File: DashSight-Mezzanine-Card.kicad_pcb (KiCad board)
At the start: 2 copper layers, 75.1 x 78.5 mm, 70 parts, among them IC1 XM1110, IC2 ELM327, J1 Pi2 Connector, J2 Euler Connector, J3 Conn_Coaxial, J4 OBD2-DB9_Male, Q1 2N3904, Q2 2N3906, Q3 2N3906, Q4 2N3904, Q5 2N3904, Q6 2N3904, Q7 2N3904, U1 MCP2561-E/P, U2 LM317L_TO92, U3 LM1085-5.0, U4 ADuM1201AR, Y1 4.0MHz

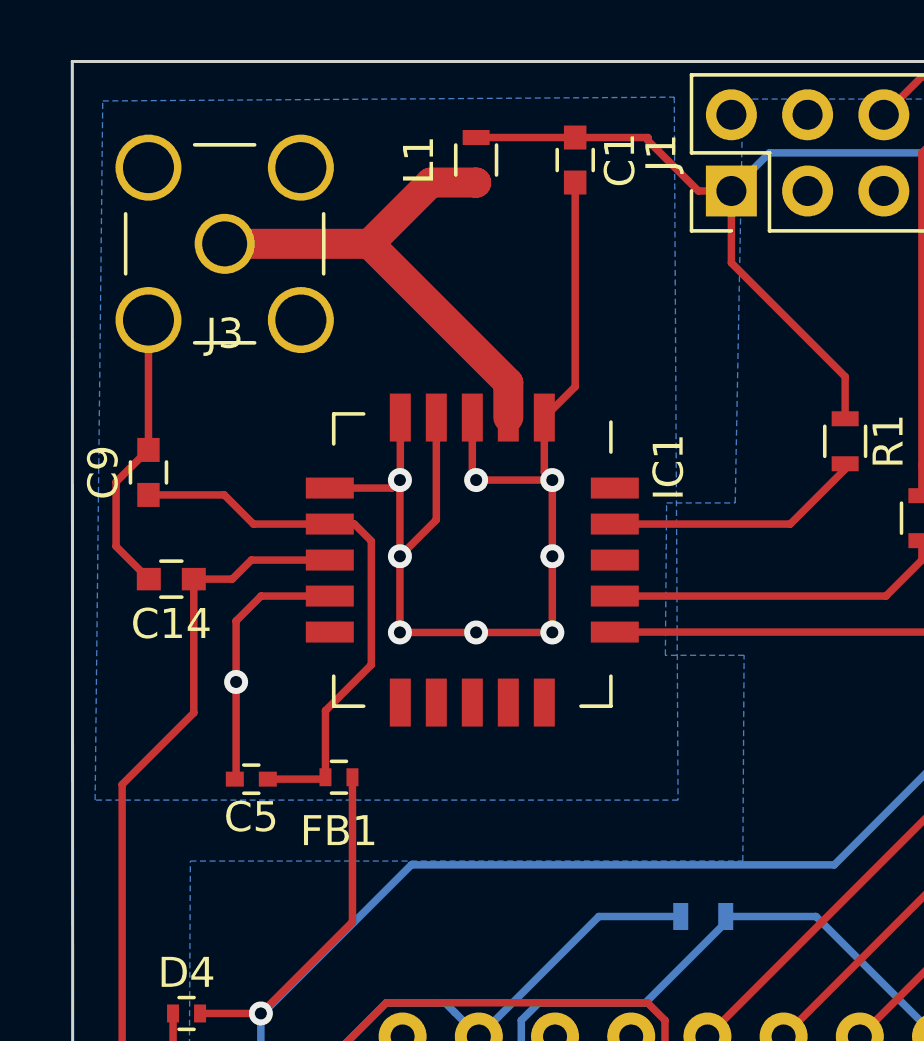
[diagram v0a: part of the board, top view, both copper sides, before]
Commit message: pcb: Update GPS layout
Signed-off-by: Alistair Francis <alistair@alistair23.me>
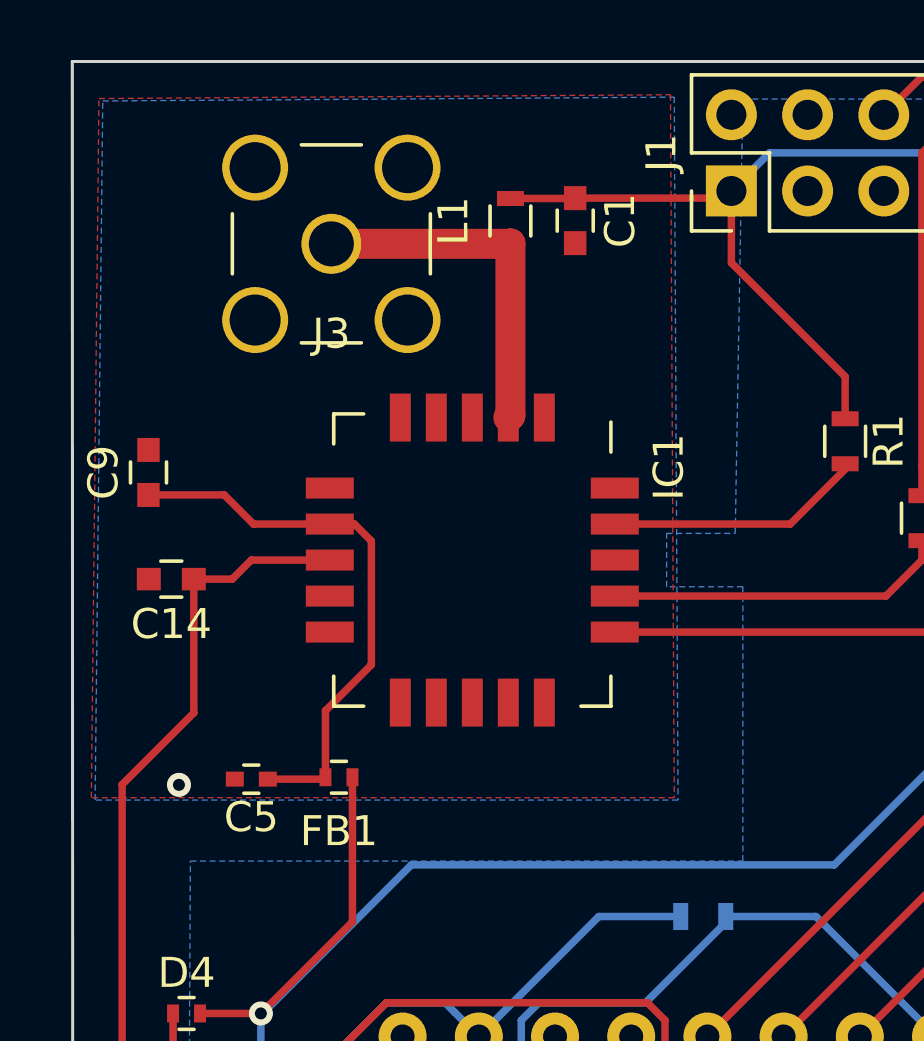
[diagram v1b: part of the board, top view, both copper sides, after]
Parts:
- moved J3 3.56 mm to (133.6, 52.6)
- moved L1 2.33 mm to (139.6, 51.8)
- moved C1 2.02 mm to (141.7, 51.8)
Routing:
- net GND: track 345.5 -> 287.2 mm, vias 17 -> 9
- net Net-(IC1-Pad2): track 16.9 -> 11.8 mm
- net +3V3: track 150.9 -> 149.1 mm
- added copper zone on F.Cu, net GND

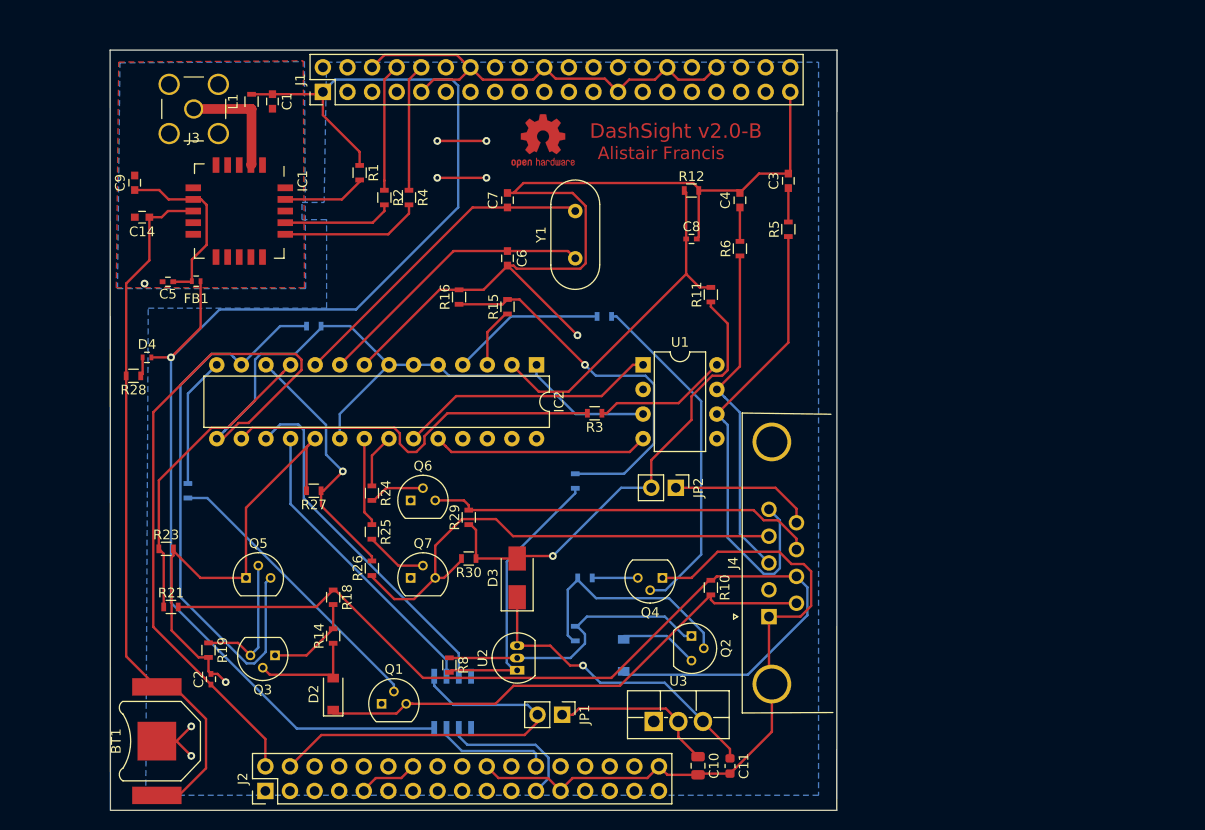
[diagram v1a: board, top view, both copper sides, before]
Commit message: pcb: Consolidate PCB layout
Signed-off-by: Alistair Francis <alistair@alistair23.me>
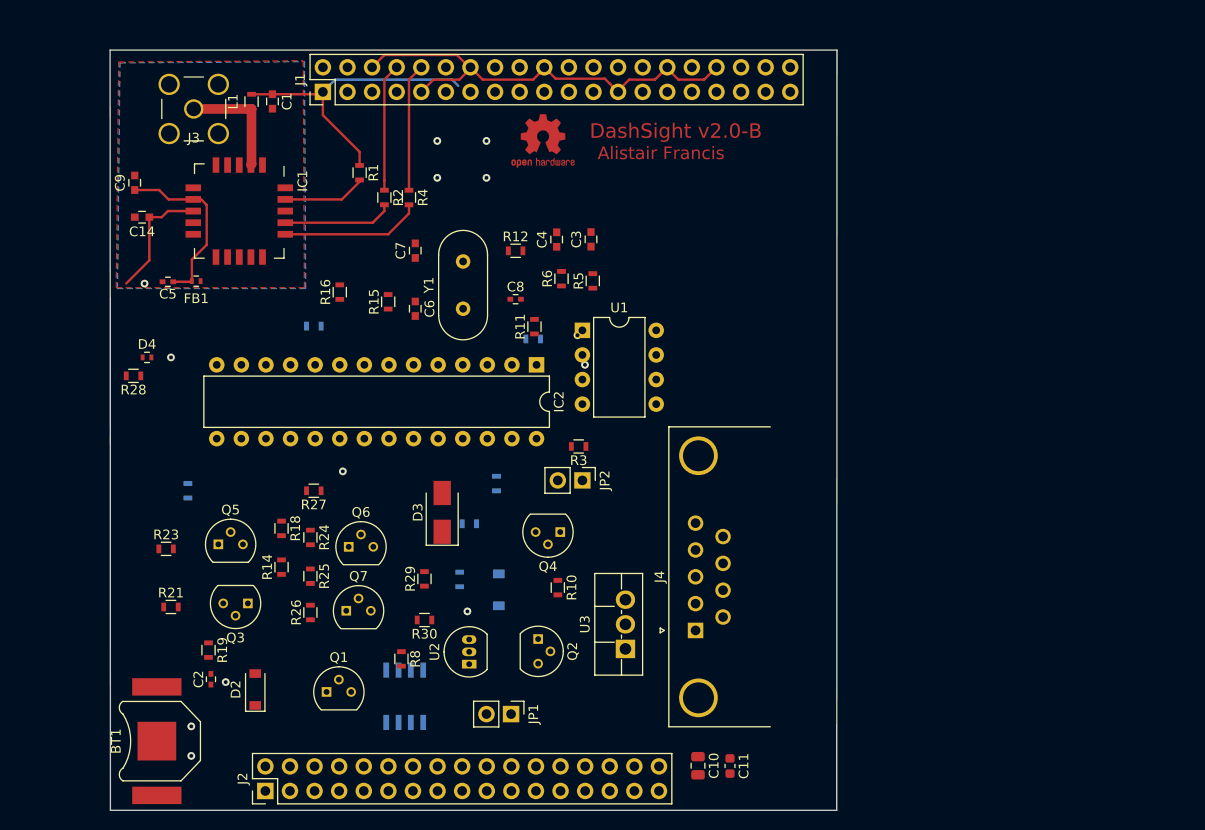
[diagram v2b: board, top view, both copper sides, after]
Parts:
- J4: footprint DashSight-PCB-Footprints:OBD2-Connector -> Connector_Dsub:DSUB-9_Male_Horizontal_P2.77x2.84mm_EdgePinOffset4.94mm_Housed_MountingHolesOffset7.48mm
- moved C3 21.3 mm to (174.6, 66.0)
- moved R5 20.9 mm to (174.8, 70.3)
- moved C4 19.4 mm to (171.1, 66.1)
- moved C8 19.2 mm to (166.8, 72.2)
- moved R12 19.2 mm to (166.8, 67.2)
- moved R6 18.7 mm to (171.6, 70.1)
- moved R11 18.5 mm to (168.8, 75.1)
- moved Q2 15.8 mm to (169.2, 107.3)
- moved R10 15.8 mm to (171.2, 102.0)
- moved D1 14.6 mm to (165.1, 102.2)
- moved R17 13.2 mm to (162.1, 95.4)
- moved R9 13.2 mm to (161.1, 101.2)
- moved Y1 12.7 mm to (161.4, 73.2)
- moved R15 12.3 mm to (153.7, 72.5)
- moved R16 12.3 mm to (148.7, 71.5)
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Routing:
- net GND: track 287.2 -> 47.4 mm, vias 9 -> 8
- net +5V: track 179.4 -> 0.00 mm
- net +3V3: track 149.1 -> 31.4 mm
- net J1850_Bus+: track 98.7 -> 0.00 mm
- net Net-(BT1-Pad1): track 73.4 -> 12.6 mm
- net Net-(IC2-Pad13): track 58.4 -> 0.00 mm
- net J1850_Bus-: track 54.5 -> 0.00 mm
- net ISO9141-2_K: track 51.8 -> 0.00 mm
- net Vbat: track 48.8 -> 0.00 mm, vias 1 -> 0
- net CAN_Low: track 48.3 -> 0.00 mm
- net ISO9141-2_L: track 40.4 -> 0.00 mm
- net PwrCntrl: track 40.0 -> 0.00 mm
- net Net-(R13-Pad2): track 39.5 -> 0.00 mm
- net Net-(IC2-Pad17): track 36.8 -> 0.00 mm
- net Net-(C8-Pad1): track 36.0 -> 0.00 mm
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
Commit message: pcb: Shrink the board
Signed-off-by: Alistair Francis <alistair@alistair23.me>
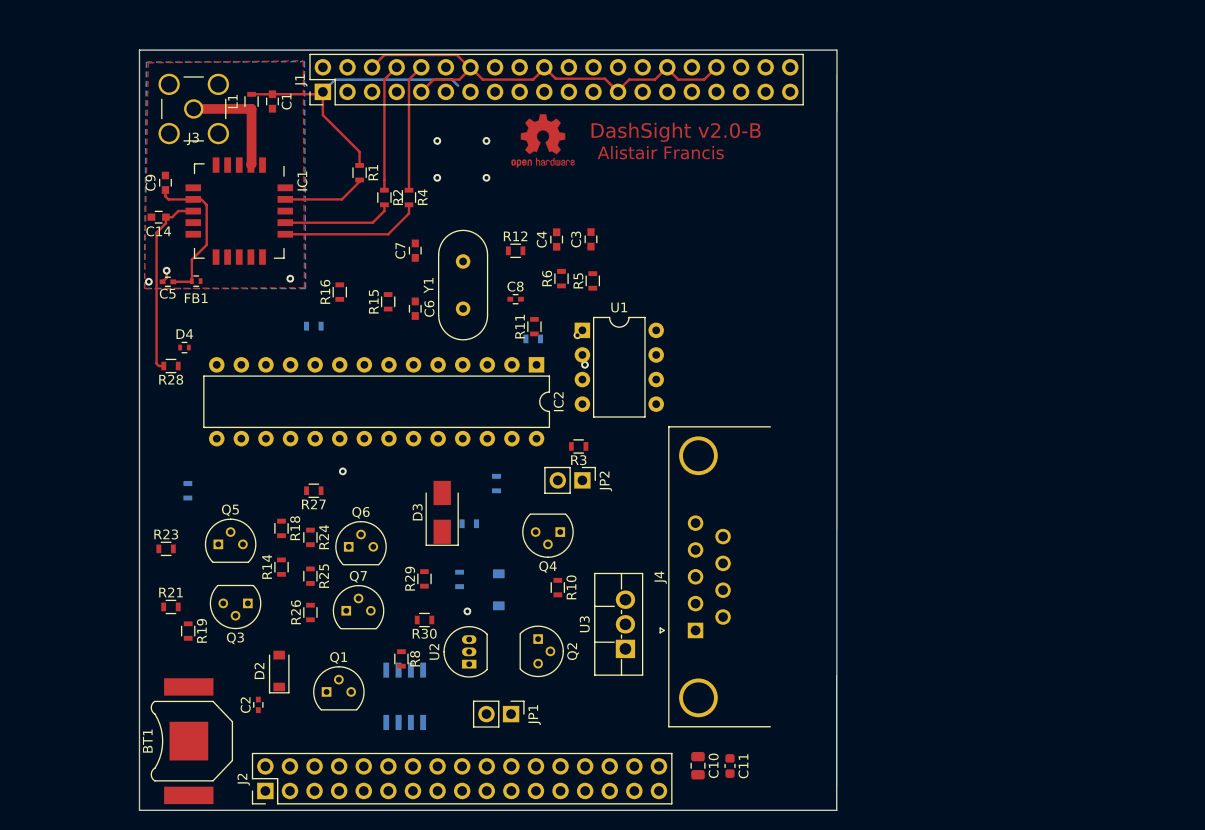
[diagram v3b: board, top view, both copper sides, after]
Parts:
- moved C2 5.56 mm to (140.3, 114.1)
- moved D4 4.00 mm to (132.7, 77.2)
- moved R28 4.00 mm to (131.3, 79.1)
- moved BT1 3.30 mm to (133.1, 117.9)
- moved C9 3.17 mm to (130.7, 60.2)
- moved D2 3.12 mm to (142.4, 110.6)
- moved R19 2.88 mm to (133.0, 106.5)
- moved C14 1.71 mm to (130.0, 63.8)
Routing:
- net Net-(BT1-Pad1): track 12.6 -> 19.5 mm
- net Net-(C5-Pad1): track 19.8 -> 16.7 mm
- net GND: track 47.4 -> 48.7 mm, vias 8 -> 7
- net +3V3: vias 1 -> 0
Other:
- board size 75.1 x 78.5 mm -> 72 x 78.5 mm
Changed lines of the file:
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@@
     (thickness 1.6)
     (drawings 6)
-    (tracks 91)
+    (tracks 93)
     (zones 0)
     (modules 70)
@@
     (solder_mask_min_width 0.25)
     (aux_axis_origin 0 0)
-    (visible_elements 7EFFA6E7)
+    (visible_elements 7FFFFFFF)
     (pcbplotparams
       (layerselection 0x010f0_ffffffff)
@@
   )
   (module Resistors_SMD:R_0603 (layer F.Cu)
-    (at 135.128 108.458 270)
+    (at 133.0325 106.4895 270)
     (descr "Resistor SMD 0603, reflow soldering, Vishay (see dcrcw.pdf)")
     (tags "resistor 0603")
@@
   )
   (module Capacitors_SMD:C_0603 (layer F.Cu)
-    (at 127.508 60.198 90)
+    (at 130.683 60.198 90)
     (descr "Capacitor SMD 0603, reflow soldering, AVX (see smccp.pdf)")
     (tags "capacitor 0603")
@@
   )
   (module Capacitors_SMD:C_0603 (layer F.Cu)
-    (at 128.27 63.754 180)
+    (at 129.9845 63.754 180)
     (descr "Capacitor SMD 0603, reflow soldering, AVX (see smccp.pdf)")
     (tags "capacitor 0603")
@@
   )
   (module DashSight-PCB-Footprints:BatteryHolder_Keystone_2998_1x6.8mm (layer F.Cu)
-    (at 129.794 117.856 90)
+    (at 133.096 117.856 90)
     (descr www.keyelco.com/product-pdf.cfm?p=763)
     (tags "Keystone type 2998 battery holder")
@@
   )
   (module Resistors_SMD:R_0402 (layer F.Cu)
-    (at 128.778 78.232)
+    (at 132.6515 77.216)
     (descr "Resistor SMD 0402, reflow soldering, Vishay (see dcrcw.pdf)")
     (tags "resistor 0402")
@@
   )
   (module Diodes_SMD:D_SOD-123 (layer F.Cu)
-    (at 139.954 112.522 90)
+    (at 142.4305 110.617 90)
     (descr SOD-123)
     (tags SOD-123)
@@
   )
   (module Capacitors_SMD:C_0402 (layer F.Cu)
-    (at 135.382 111.464 90)
+    (at 140.2715 114.1095 90)
     (descr "Capacitor SMD 0402, reflow soldering, AVX (see smccp.pdf)")
     (tags "capacitor 0402")
@@
   )
   (module Resistors_SMD:R_0603 (layer F.Cu)
-    (at 127.381 80.137 180)
+    (at 131.2545 79.121 180)
     (descr "Resistor SMD 0603, reflow soldering, Vishay (see dcrcw.pdf)")
     (tags "resistor 0603")
@@
     (effects (font (size 1.5 1.5) (thickness 0.3)))
   )
-  (gr_line (start 125 125) (end 124.968 46.5) (layer Edge.Cuts) (width 0.1))
-  (gr_line (start 200 125) (end 125 125) (layer Edge.Cuts) (width 0.1))
+  (gr_line (start 128 125) (end 128 46.5) (layer Edge.Cuts) (width 0.1))
+  (gr_line (start 200 125) (end 128 125) (layer Edge.Cuts) (width 0.1))
   (gr_line (start 200.025 46.5) (end 200 125) (layer Edge.Cuts) (width 0.1))
-  (gr_line (start 124.968 46.5) (end 200.025 46.5) (layer Edge.Cuts) (width 0.1))
-  (via (at 128.524 70.612) (size 0.8) (drill 0.4) (layers F.Cu B.Cu) (net 1))
+  (gr_line (start 128 46.5) (end 200 46.5) (layer Edge.Cuts) (width 0.1))
   (segment (start 195.26 50.877) (end 195.199 50.816) (width 0.25) (layer F.Cu) (net 1) (status 30))
-  (segment (start 127.508 59.448) (end 127.496 59.448) (width 0.25) (layer F.Cu) (net 1) (status 30))
-  (via (at 173.228 75.946) (size 0.8) (drill 0.4) (layers F.Cu B.Cu) (net 96))
-  (via (at 136.906 111.76) (size 0.8) (drill 0.4) (layers F.Cu B.Cu) (net 1))
+  (segment (start 129.2225 59.448) (end 129.2105 59.448) (width 0.25) (layer F.Cu) (net 1) (status 30))
   (segment (start 177.419 50.816) (end 177.419 50.689) (width 0.25) (layer F.Cu) (net 1) (status 30))
   (segment (start 182.499 48.276) (end 182.499 48.403) (width 0.25) (layer F.Cu) (net 1) (status 30))
@@
   (via (at 158.75 59.69) (size 0.8) (drill 0.4) (layers F.Cu B.Cu) (net 1))
   (via (at 163.83 59.69) (size 0.8) (drill 0.4) (layers F.Cu B.Cu) (net 1))
-  (via (at 133.35 116.332) (size 0.8) (drill 0.4) (layers F.Cu B.Cu) (net 1))
-  (via (at 133.35 119.38) (size 0.8) (drill 0.4) (layers F.Cu B.Cu) (net 1))
   (segment (start 158.369 49.546) (end 157.099 50.816) (width 0.25) (layer F.Cu) (net 1) (status 20))
   (segment (start 162.179 48.403) (end 161.036 49.546) (width 0.25) (layer F.Cu) (net 1) (status 10))
@@
   (segment (start 170.974001 49.451001) (end 176.054001 49.451001) (width 0.25) (layer F.Cu) (net 1))
   (segment (start 169.799 48.276) (end 170.974001 49.451001) (width 0.25) (layer F.Cu) (net 1))
+  (via (at 143.5735 70.104) (size 0.8) (drill 0.4) (layers F.Cu B.Cu) (net 1))
+  (via (at 130.81 69.2785) (size 0.8) (drill 0.4) (layers F.Cu B.Cu) (net 1))
+  (via (at 128.9685 70.4215) (size 0.8) (drill 0.4) (layers F.Cu B.Cu) (net 1))
+  (segment (start 130.81 69.9985) (end 130.387 70.4215) (width 0.25) (layer F.Cu) (net 1))
+  (segment (start 130.81 69.2785) (end 130.81 69.9985) (width 0.25) (layer F.Cu) (net 1))
   (via (at 161.8615 104.4575) (size 0.8) (drill 0.4) (layers F.Cu B.Cu) (net 17))
   (segment (start 157.099 48.276) (end 155.829 49.546) (width 0.25) (layer F.Cu) (net 19) (status 10))
@@
   (segment (start 155.829 60.972) (end 155.829 59.956) (width 0.25) (layer F.Cu) (net 19))
   (via (at 174 79) (size 0.8) (drill 0.4) (layers F.Cu B.Cu) (net 27))
-  (via (at 131.2545 78.232) (size 0.8) (drill 0.4) (layers F.Cu B.Cu) (net 35))
   (segment (start 160.909 50.181) (end 160.274 49.546) (width 0.25) (layer B.Cu) (net 35))
   (segment (start 148.209 49.546) (end 146.939 50.816) (width 0.25) (layer B.Cu) (net 35) (status 20))
@@
   (segment (start 153.289 59.956) (end 153.289 49.53) (width 0.25) (layer F.Cu) (net 62))
   (segment (start 153.289 60.972) (end 153.289 59.956) (width 0.25) (layer F.Cu) (net 62))
+  (via (at 173.228 75.946) (size 0.8) (drill 0.4) (layers F.Cu B.Cu) (net 96))
   (segment (start 155.829 62.472) (end 155.829 62.484) (width 0.25) (layer F.Cu) (net 106) (status 30))
   (segment (start 155.829 62.472) (end 155.829 63.373) (width 0.25) (layer F.Cu) (net 106) (status 10))
@@
   (segment (start 148.901 61.919) (end 143.053 61.919) (width 0.25) (layer F.Cu) (net 109) (status 20))
   (segment (start 150.731 60.089) (end 148.901 61.919) (width 0.25) (layer F.Cu) (net 109) (status 10))
-  (segment (start 129.02 63.754) (end 129.02 68.211) (width 0.25) (layer F.Cu) (net 110) (status 10))
-  (segment (start 129.02 68.211) (end 126.631 70.6) (width 0.25) (layer F.Cu) (net 110))
-  (segment (start 129.02 63.754) (end 130.302 63.754) (width 0.25) (layer F.Cu) (net 110) (status 10))
-  (segment (start 130.937 63.119) (end 133.553 63.119) (width 0.25) (layer F.Cu) (net 110) (status 20))
-  (segment (start 130.302 63.754) (end 130.937 63.119) (width 0.25) (layer F.Cu) (net 110))
+  (segment (start 132.0195 63.119) (end 132.503 63.119) (width 0.25) (layer F.Cu) (net 110))
+  (segment (start 131.3845 63.754) (end 132.0195 63.119) (width 0.25) (layer F.Cu) (net 110))
+  (segment (start 132.503 63.119) (end 133.553 63.119) (width 0.25) (layer F.Cu) (net 110))
+  (segment (start 130.7345 63.754) (end 131.3845 63.754) (width 0.25) (layer F.Cu) (net 110))
+  (segment (start 129.761999 78.878499) (end 130.0045 79.121) (width 0.25) (layer F.Cu) (net 110))
+  (segment (start 129.761999 65.351501) (end 129.761999 78.878499) (width 0.25) (layer F.Cu) (net 110))
+  (segment (start 130.7345 64.379) (end 129.761999 65.351501) (width 0.25) (layer F.Cu) (net 110))
+  (segment (start 130.0045 79.121) (end 130.5045 79.121) (width 0.25) (layer F.Cu) (net 110))
+  (segment (start 130.7345 63.754) (end 130.7345 64.379) (width 0.25) (layer F.Cu) (net 110))
   (segment (start 133.344 61.71) (end 133.553 61.919) (width 0.25) (layer F.Cu) (net 111) (status 30))
-  (segment (start 127.508 60.948) (end 127.508 60.96) (width 0.25) (layer F.Cu) (net 111) (status 30))
-  (segment (start 127.717 61.157) (end 127.508 60.948) (width 0.25) (layer F.Cu) (net 111) (status 30))
   (segment (start 133.553 61.919) (end 134.2455 61.919) (width 0.25) (layer F.Cu) (net 111) (status 30))
   (segment (start 133.3445 70.4215) (end 133.408 70.358) (width 0.25) (layer F.Cu) (net 111) (status 30))
@@
   (segment (start 134.9375 66.6115) (end 134.9375 62.484) (width 0.25) (layer F.Cu) (net 111))
   (segment (start 133.408 68.141) (end 134.9375 66.6115) (width 0.25) (layer F.Cu) (net 111))
-  (segment (start 127.508 60.948) (end 130.036 60.948) (width 0.25) (layer F.Cu) (net 111) (status 10))
-  (segment (start 131.007 61.919) (end 133.553 61.919) (width 0.25) (layer F.Cu) (net 111) (status 20))
-  (segment (start 130.036 60.948) (end 131.007 61.919) (width 0.25) (layer F.Cu) (net 111))
   (segment (start 133.408 68.141) (end 133.408 70.358) (width 0.25) (layer F.Cu) (net 111) (status 20))
+  (segment (start 130.683 61.598) (end 130.683 60.948) (width 0.25) (layer F.Cu) (net 111))
+  (segment (start 131.004 61.919) (end 130.683 61.598) (width 0.25) (layer F.Cu) (net 111))
+  (segment (start 133.553 61.919) (end 131.004 61.919) (width 0.25) (layer F.Cu) (net 111))
   (segment (start 139.561 52.578) (end 139.573 52.566) (width 1) (layer F.Cu) (net 113))
   (segment (start 133.604 52.578) (end 139.561 52.578) (width 1) (layer F.Cu) (net 113))
@@
     (polygon
       (pts
-        (xy 125.984 47.8155) (xy 145.034 47.6885) (xy 145.161 71.12) (xy 125.73 71.12)
+        (xy 128.7145 47.752) (xy 145.034 47.6885) (xy 145.161 71.12) (xy 128.524 71.12)
       )
     )
@@
     (polygon
       (pts
-        (xy 125.85753 47.73513) (xy 144.90753 47.60813) (xy 145.03453 71.03963) (xy 125.60353 71.03963)
+        (xy 128.905 47.8155) (xy 144.90753 47.60813) (xy 145.03453 71.03963) (xy 128.524 71.12)
       )
     )
